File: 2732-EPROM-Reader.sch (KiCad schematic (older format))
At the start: 3 parts, among them U1 ATMEGA328P-P, U2 2732, U3 4040

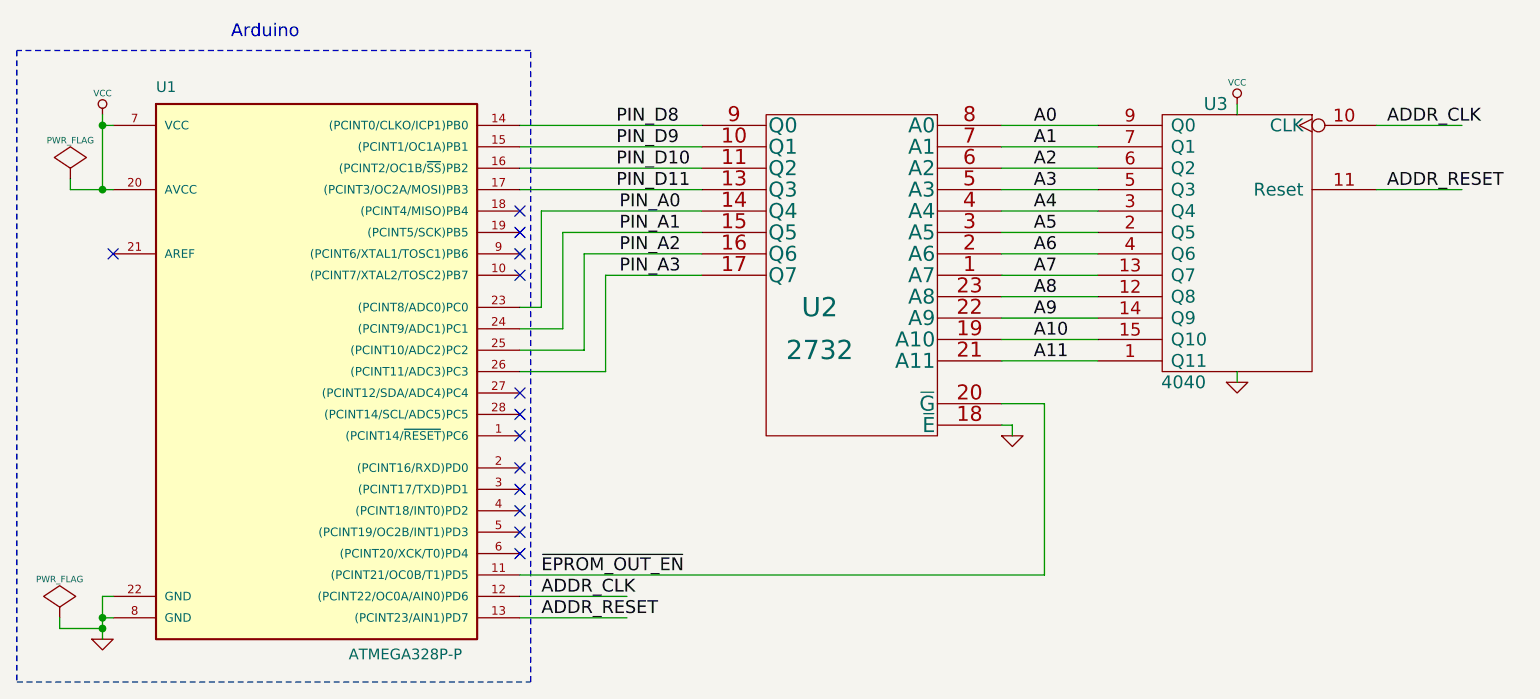
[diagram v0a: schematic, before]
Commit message: Added decoupling caps!
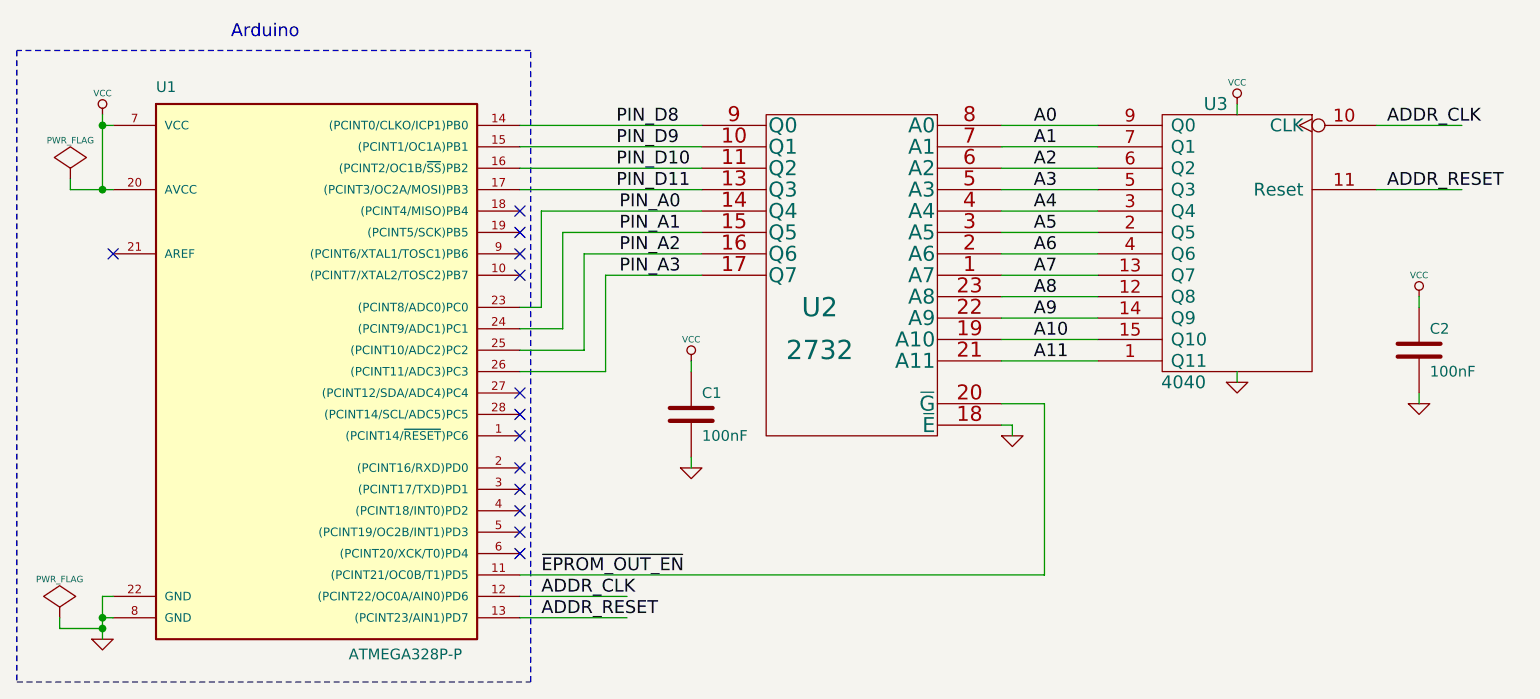
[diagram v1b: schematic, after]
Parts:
- added C1, C2: 100nF, symbol C
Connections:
- wire segments 48 -> 52
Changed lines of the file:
@@
-EESchema Schematic File Version 2  date Sat 06 Oct 2012 08:50:57 PM EEST
+EESchema Schematic File Version 2  date Sun 07 Oct 2012 09:41:09 PM EEST
 LIBS:power
 LIBS:device
@@
 Sheet 1 1
 Title ""
-Date "6 oct 2012"
+Date "7 oct 2012"
 Rev ""
 Comp ""
@@
 Text Label 8250 4400 0    60   ~ 0
 A11
+$Comp
+L C C2
+U 1 1 5071CCD9
+P 10050 4350
+F 0 "C2" H 10100 4450 50  0000 L CNN
+F 1 "100nF" H 10100 4250 50  0000 L CNN
+	1    10050 4350
+	1    0    0    -1
+$EndComp
+$Comp
+L VCC #PWR?
+U 1 1 5071CCE6
+P 10050 4100
+F 0 "#PWR?" H 10050 4200 30  0001 C CNN
+F 1 "VCC" H 10050 4200 30  0000 C CNN
+	1    10050 4100
+	1    0    0    -1
+$EndComp
+$Comp
+L GND #PWR?
+U 1 1 5071CCEC
+P 10050 4600
+F 0 "#PWR?" H 10050 4600 30  0001 C CNN
+F 1 "GND" H 10050 4530 30  0001 C CNN
+	1    10050 4600
+	1    0    0    -1
+$EndComp
+Wire Wire Line
+	10050 4600 10050 4550
+Wire Wire Line
+	10050 4150 10050 4100
+$Comp
+L C C1
+U 1 1 5071CD6A
+P 6650 4650
+F 0 "C1" H 6700 4750 50  0000 L CNN
+F 1 "100nF" H 6700 4550 50  0000 L CNN
+	1    6650 4650
+	1    0    0    -1
+$EndComp
+$Comp
+L VCC #PWR?
+U 1 1 5071CD70
+P 6650 4400
+F 0 "#PWR?" H 6650 4500 30  0001 C CNN
+F 1 "VCC" H 6650 4500 30  0000 C CNN
+	1    6650 4400
+	1    0    0    -1
+$EndComp
+$Comp
+L GND #PWR?
+U 1 1 5071CD76
+P 6650 4900
+F 0 "#PWR?" H 6650 4900 30  0001 C CNN
+F 1 "GND" H 6650 4830 30  0001 C CNN
+	1    6650 4900
+	1    0    0    -1
+$EndComp
+Wire Wire Line
+	6650 4900 6650 4850
+Wire Wire Line
+	6650 4450 6650 4400
 $EndSCHEMATC
